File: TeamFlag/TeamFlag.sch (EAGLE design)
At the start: 18 parts, among them Q1 IRFML8244, Q2 IRFML8244

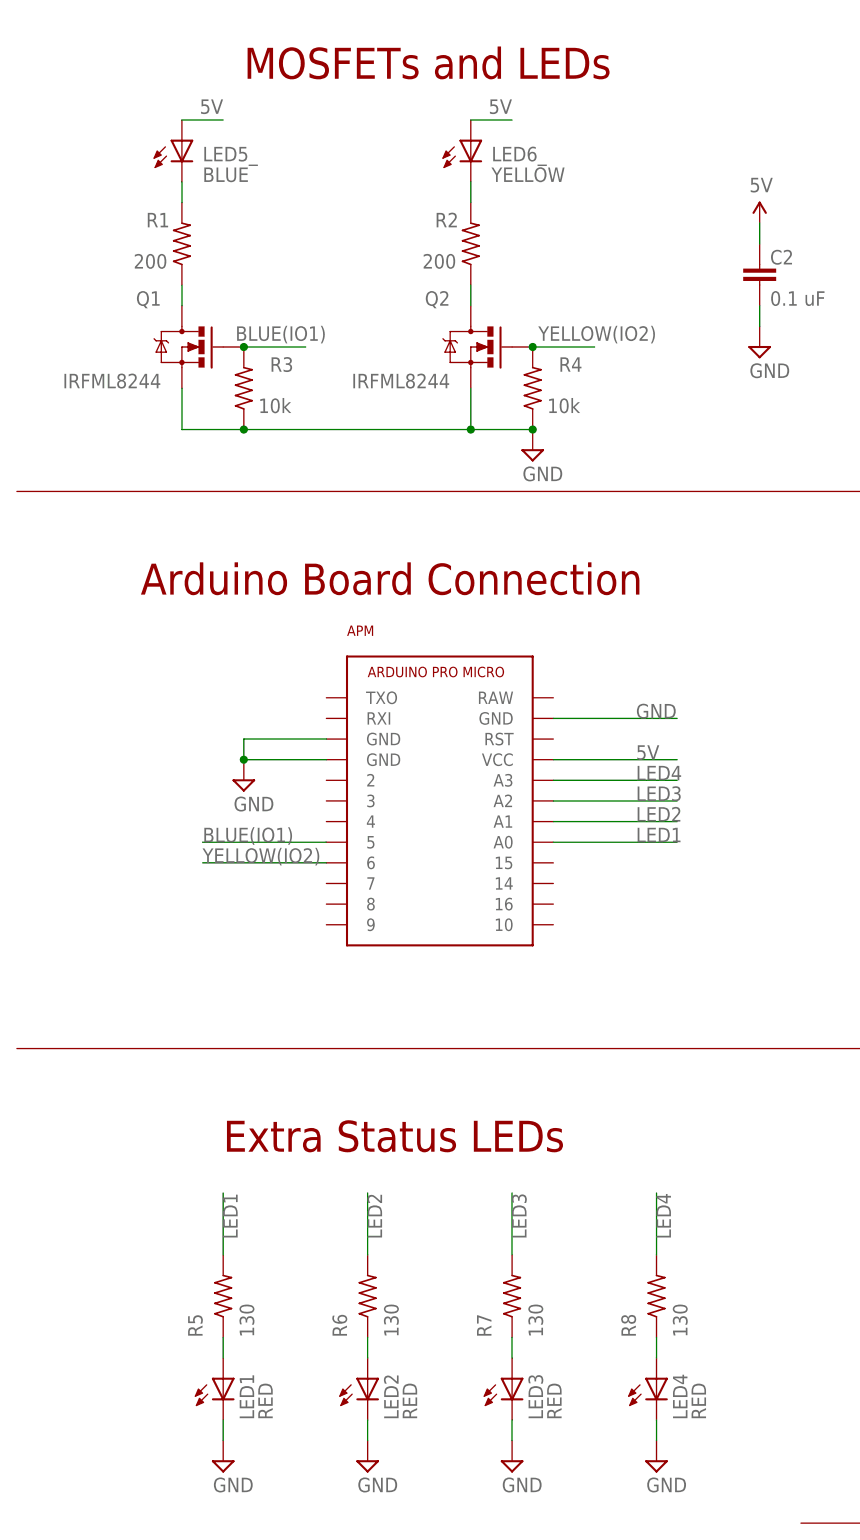
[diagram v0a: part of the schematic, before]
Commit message: Replace the apm with surface mount; needs routing
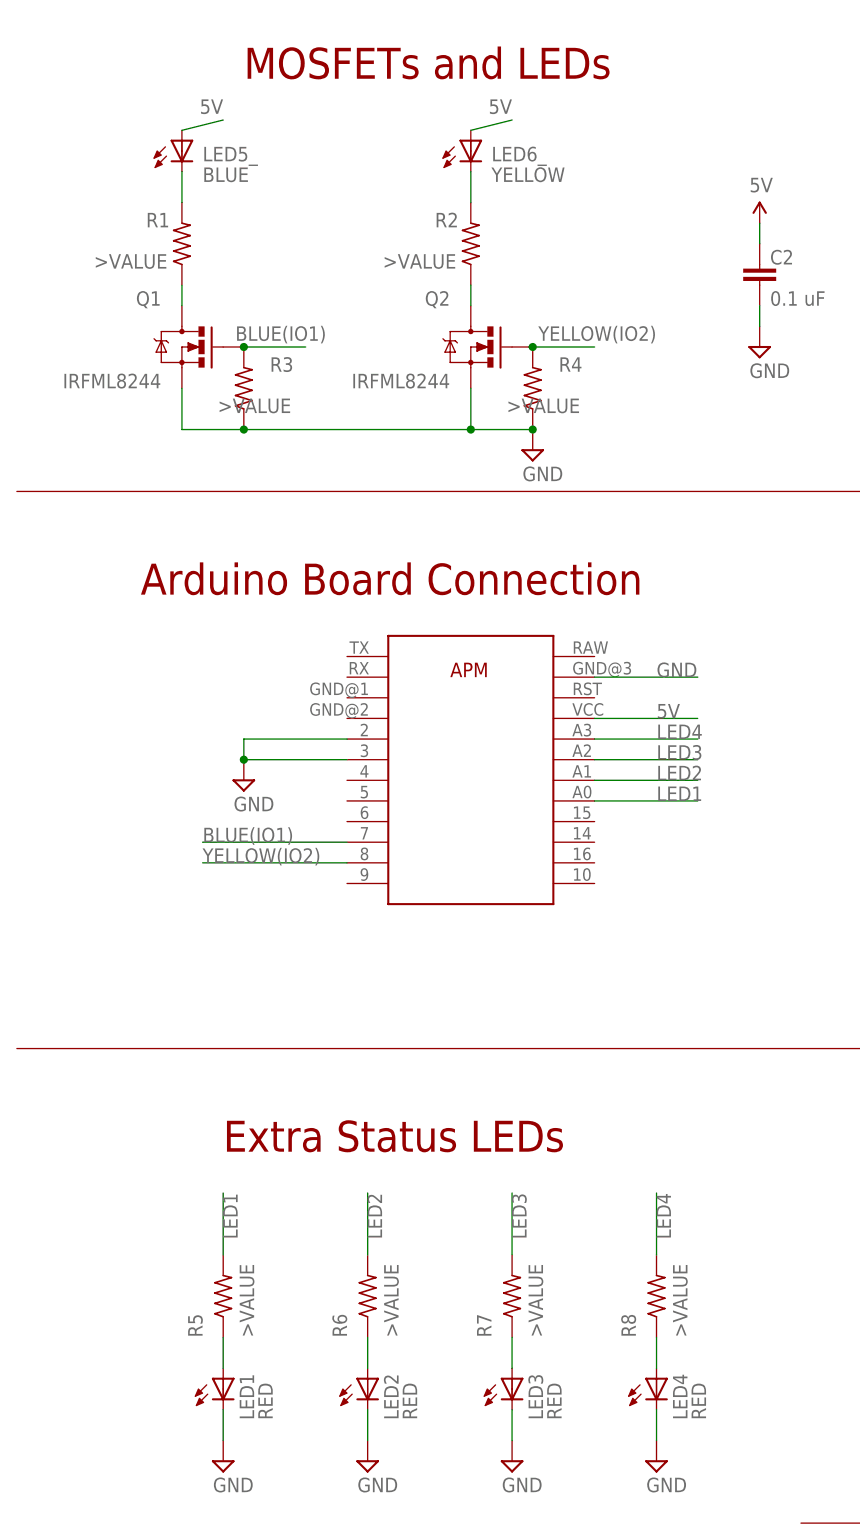
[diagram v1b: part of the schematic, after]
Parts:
- removed APM: ARDUINO_PRO_MICRO, pie:ARDUINO_PRO_MICRO
- added IC1: ARDUINO_PRO_MICRO_SM, pie:ARDUINO_PRO_MICRO_SM
- R1, R2: value 200 -> >VALUE
- R3, R4: value 10k -> >VALUE
- R5, R6, R7, R8: value 130 -> >VALUE
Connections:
- net 5V: now also IC1.VCC; no longer APM.VCC
- net BLUE(IO1): now also IC1.7; no longer APM.5
- net GND: now also IC1.2, IC1.3, IC1.GND@3; no longer APM.GND@0, APM.GND@1, APM.GND@2
- net LED1: now also IC1.A0; no longer APM.A0
- net LED2: now also IC1.A1; no longer APM.A1
- net LED3: now also IC1.A2; no longer APM.A2
- net LED4: now also IC1.A3; no longer APM.A3
- net YELLOW(IO2): now also IC1.8; no longer APM.6

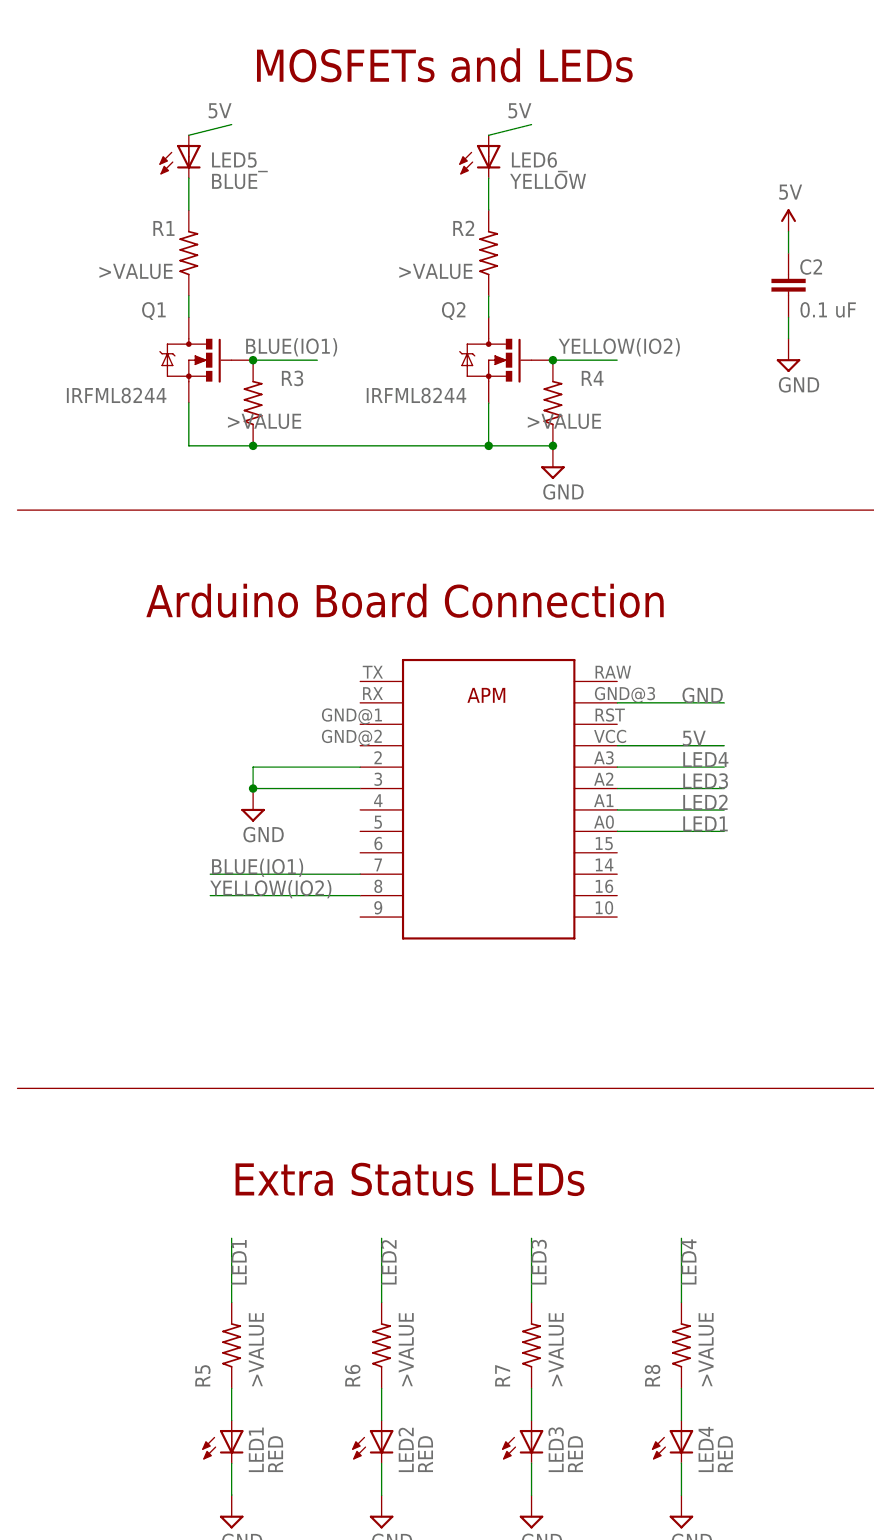
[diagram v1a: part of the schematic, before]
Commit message: Route surface mount apm on teamflag
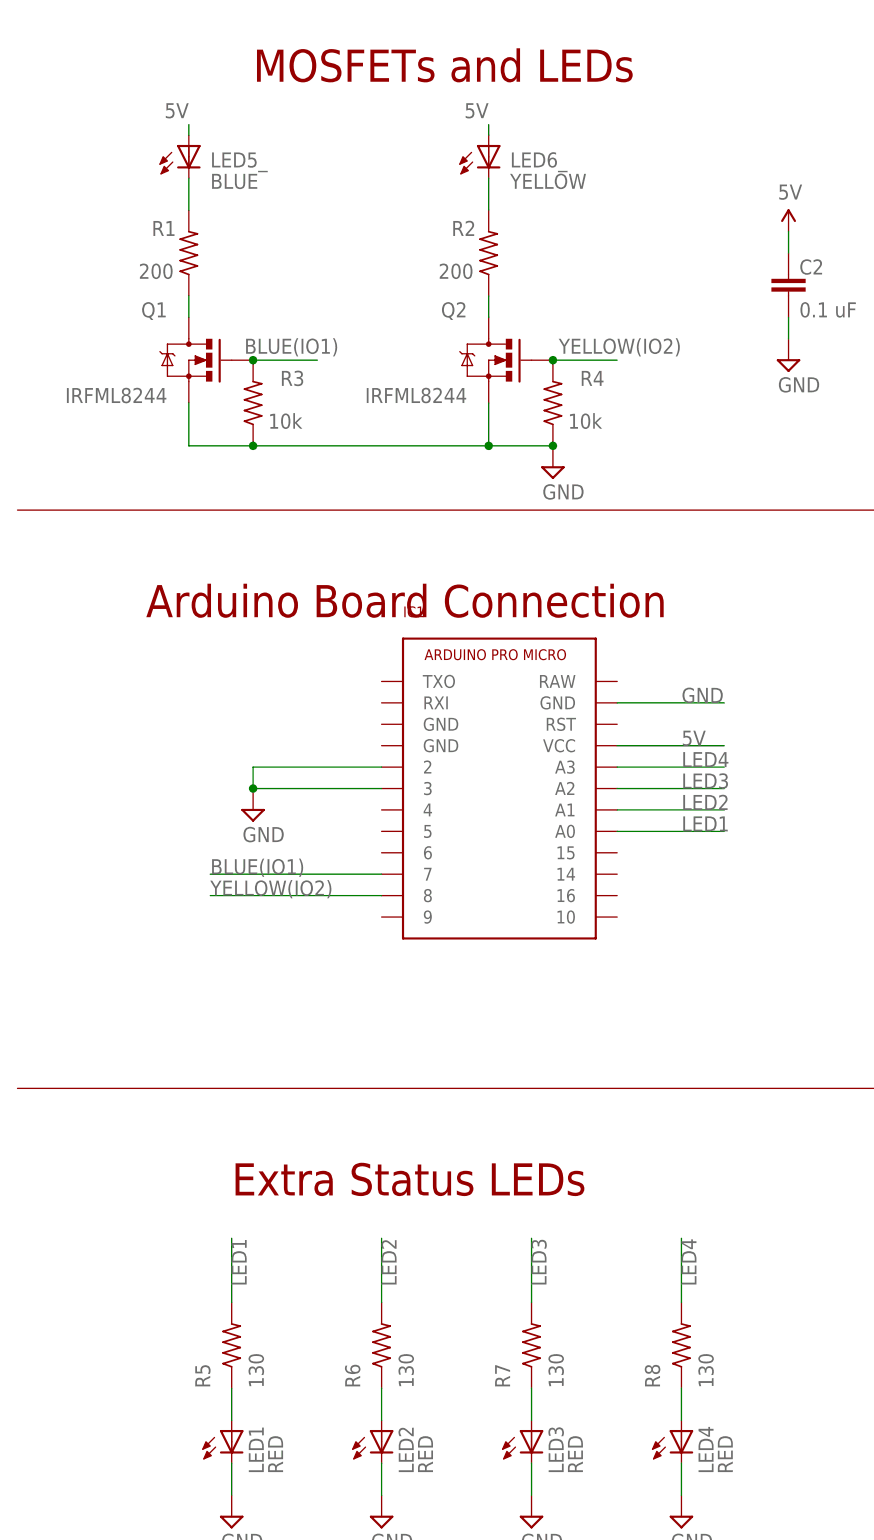
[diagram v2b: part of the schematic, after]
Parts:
- IC1: value ARDUINO_PRO_MICRO_SM -> ARDUINO_PRO_MICROSMD; device pie:ARDUINO_PRO_MICRO_SM -> pie:ARDUINO_PRO_MICROSMD
- R1, R2: value >VALUE -> 200
- R3, R4: value >VALUE -> 10k
- R5, R6, R7, R8: value >VALUE -> 130
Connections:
- net GND: now also IC1.GND@2; no longer IC1.GND@3
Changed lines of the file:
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@@
 <?xml version="1.0" encoding="utf-8"?>
 <!DOCTYPE eagle SYSTEM "eagle.dtd">
-<eagle version="7.7.0">
+<eagle version="7.6.0">
 <drawing>
 <settings>
@@
 <part name="LED5_" library="pie" deviceset="LED" device="LED5MM-NOFLAT" value="BLUE"/>
 <part name="LED6_" library="pie" deviceset="LED" device="LED5MM-NOFLAT" value="YELLOW"/>
-<part name="R1" library="pie" deviceset="R-US_" device="R0603" value="&gt;VALUE"/>
-<part name="R2" library="pie" deviceset="R-US_" device="R0603" value="&gt;VALUE"/>
+<part name="R1" library="pie" deviceset="R-US_" device="R0603" value="200"/>
+<part name="R2" library="pie" deviceset="R-US_" device="R0603" value="200"/>
 <part name="Q1" library="pie" deviceset="MOSFET-NCHANNEL" device="SMD" value="IRFML8244"/>
 <part name="Q2" library="pie" deviceset="MOSFET-NCHANNEL" device="SMD" value="IRFML8244"/>
@@
 <attribute name="REVISION" value="9B"/>
 </part>
-<part name="R3" library="pie" deviceset="R-US_" device="R0603" value="&gt;VALUE"/>
-<part name="R4" library="pie" deviceset="R-US_" device="R0603" value="&gt;VALUE"/>
+<part name="R3" library="pie" deviceset="R-US_" device="R0603" value="10k"/>
+<part name="R4" library="pie" deviceset="R-US_" device="R0603" value="10k"/>
 <part name="C2" library="pie" deviceset="CAP" device="0603-CAP" value="0.1 uF"/>
 <part name="U$6" library="pie" deviceset="5V" device=""/>
 <part name="SUPPLY4" library="pie" deviceset="GND" device=""/>
-<part name="R5" library="pie" deviceset="R-US_" device="R0603" value="&gt;VALUE"/>
+<part name="R5" library="pie" deviceset="R-US_" device="R0603" value="130"/>
 <part name="LED1" library="pie" deviceset="LED" device="0805" value="RED"/>
 <part name="SUPPLY15" library="pie" deviceset="GND" device=""/>
-<part name="R6" library="pie" deviceset="R-US_" device="R0603" value="&gt;VALUE"/>
+<part name="R6" library="pie" deviceset="R-US_" device="R0603" value="130"/>
 <part name="LED2" library="pie" deviceset="LED" device="0805" value="RED"/>
 <part name="SUPPLY2" library="pie" deviceset="GND" device=""/>
-<part name="R7" library="pie" deviceset="R-US_" device="R0603" value="&gt;VALUE"/>
+<part name="R7" library="pie" deviceset="R-US_" device="R0603" value="130"/>
 <part name="LED3" library="pie" deviceset="LED" device="0805" value="RED"/>
 <part name="SUPPLY3" library="pie" deviceset="GND" device=""/>
-<part name="R8" library="pie" deviceset="R-US_" device="R0603" value="&gt;VALUE"/>
+<part name="R8" library="pie" deviceset="R-US_" device="R0603" value="130"/>
 <part name="LED4" library="pie" deviceset="LED" device="0805" value="RED"/>
 <part name="SUPPLY5" library="pie" deviceset="GND" device=""/>
 <part name="SUPPLY6" library="pie" deviceset="GND" device=""/>
-<part name="IC1" library="pie" deviceset="ARDUINO_PRO_MICRO_SM" device=""/>
+<part name="IC1" library="pie" deviceset="ARDUINO_PRO_MICRO" device="SMD"/>
 </parts>
 <sheets>
@@
 <segment>
 <label x="22.86" y="81.28" size="1.778" layer="95"/>
-<wire x1="40.64" y1="81.28" x2="22.86" y2="81.28" width="0.1524" layer="91"/>
+<wire x1="43.18" y1="81.28" x2="22.86" y2="81.28" width="0.1524" layer="91"/>
 <pinref part="IC1" gate="G$1" pin="8"/>
 </segment>
@@
 <segment>
 <wire x1="27.94" y1="96.52" x2="27.94" y2="93.98" width="0.1524" layer="91"/>
-<wire x1="27.94" y1="93.98" x2="40.64" y2="93.98" width="0.1524" layer="91"/>
+<wire x1="27.94" y1="93.98" x2="43.18" y2="93.98" width="0.1524" layer="91"/>
 <pinref part="SUPPLY6" gate="GND" pin="GND"/>
 <junction x="27.94" y="93.98"/>
+<wire x1="27.94" y1="96.52" x2="43.18" y2="96.52" width="0.1524" layer="91"/>
+<pinref part="IC1" gate="G$1" pin="2"/>
 <pinref part="IC1" gate="G$1" pin="3"/>
-<pinref part="IC1" gate="G$1" pin="2"/>
-<wire x1="27.94" y1="96.52" x2="40.64" y2="96.52" width="0.1524" layer="91"/>
 </segment>
 <segment>
 <wire x1="71.12" y1="104.14" x2="83.82" y2="104.14" width="0.1524" layer="91"/>
 <label x="78.74" y="104.14" size="1.778" layer="95"/>
-<pinref part="IC1" gate="G$1" pin="GND@3"/>
+<pinref part="IC1" gate="G$1" pin="GND@2"/>
 </segment>
 </net>
@@
 <segment>
 <label x="22.86" y="83.82" size="1.778" layer="95"/>
-<wire x1="40.64" y1="83.82" x2="22.86" y2="83.82" width="0.1524" layer="91"/>
+<wire x1="43.18" y1="83.82" x2="22.86" y2="83.82" width="0.1524" layer="91"/>
 <pinref part="IC1" gate="G$1" pin="7"/>
 </segment>
@@
 </segment>
 <segment>
-<wire x1="55.88" y1="171.45" x2="60.96" y2="172.72" width="0.1524" layer="91"/>
-<label x="60.96" y="175.26" size="1.778" layer="95" rot="R180"/>
+<wire x1="55.88" y1="171.45" x2="55.88" y2="172.72" width="0.1524" layer="91"/>
+<label x="55.88" y="175.26" size="1.778" layer="95" rot="R180"/>
 <pinref part="LED6_" gate="G$1" pin="A"/>
 </segment>
 <segment>
-<wire x1="20.32" y1="171.45" x2="25.4" y2="172.72" width="0.1524" layer="91"/>
-<label x="25.4" y="175.26" size="1.778" layer="95" rot="R180"/>
+<wire x1="20.32" y1="171.45" x2="20.32" y2="172.72" width="0.1524" layer="91"/>
+<label x="20.32" y="175.26" size="1.778" layer="95" rot="R180"/>
 <pinref part="LED5_" gate="G$1" pin="A"/>
 </segment>

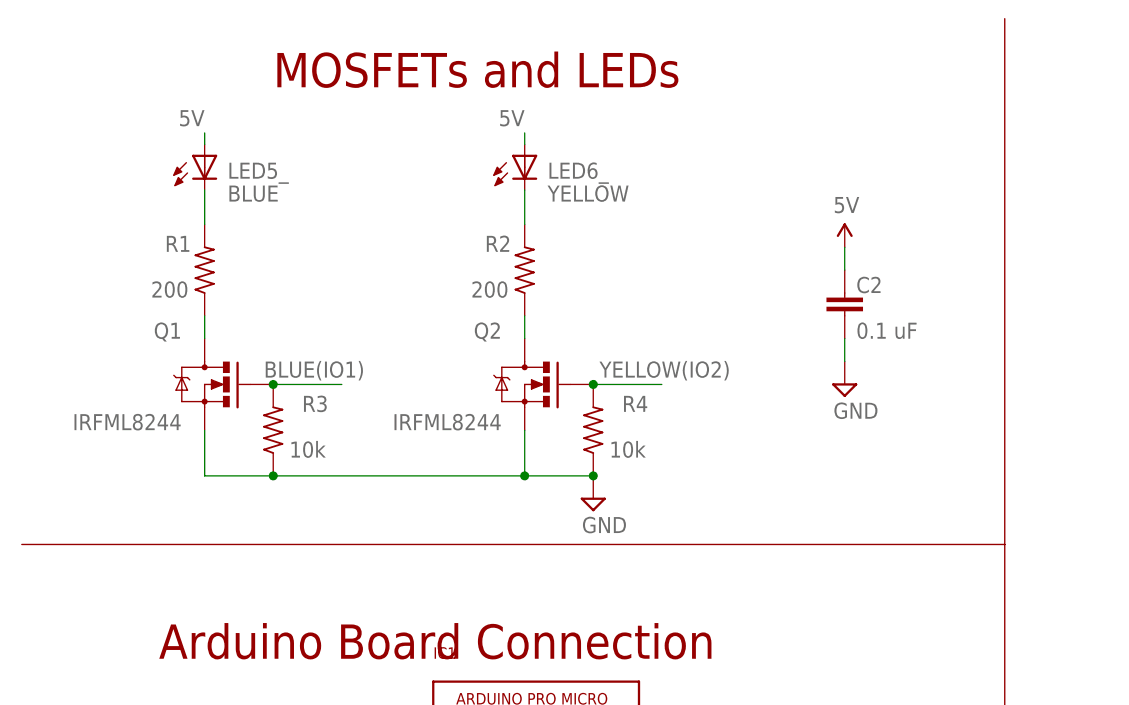
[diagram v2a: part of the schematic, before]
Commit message: Update the MOSFET part to use pie lbrs thing
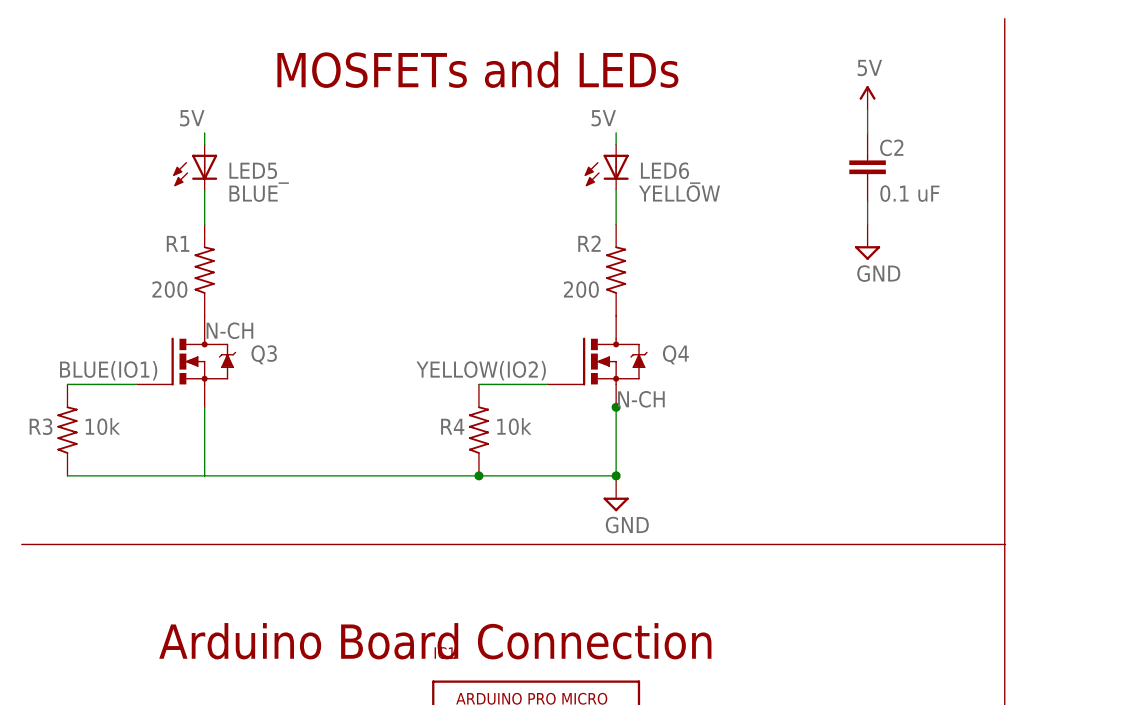
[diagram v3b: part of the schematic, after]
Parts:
- removed Q1, Q2: IRFML8244, pie:MOSFET-NCHANNELSMD
- added Q3, Q4: N-CH, pie:N-CHANNEL-MOSFETSOT23-3
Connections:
- net BLUE(IO1): now also Q3.G; no longer Q1.G
- net BSOURCE: now also Q3.D; no longer Q1.D
- net GND: now also Q3.S@2, Q4.S@2; no longer Q1.S, Q2.S
- net YELLOW(IO2): now also Q4.G; no longer Q2.G
- net YSOURCE: now also Q4.D; no longer Q2.D
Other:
- moved on the sheet: C2, LED6_, R2, R3, R4
